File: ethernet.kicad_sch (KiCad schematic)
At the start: 38 parts, among them IC1 ACPL-217-500E, J6 5-2337992-8, U22 TPS2372-3RGWR, U23 ULS-12{slash}5-D48N-C

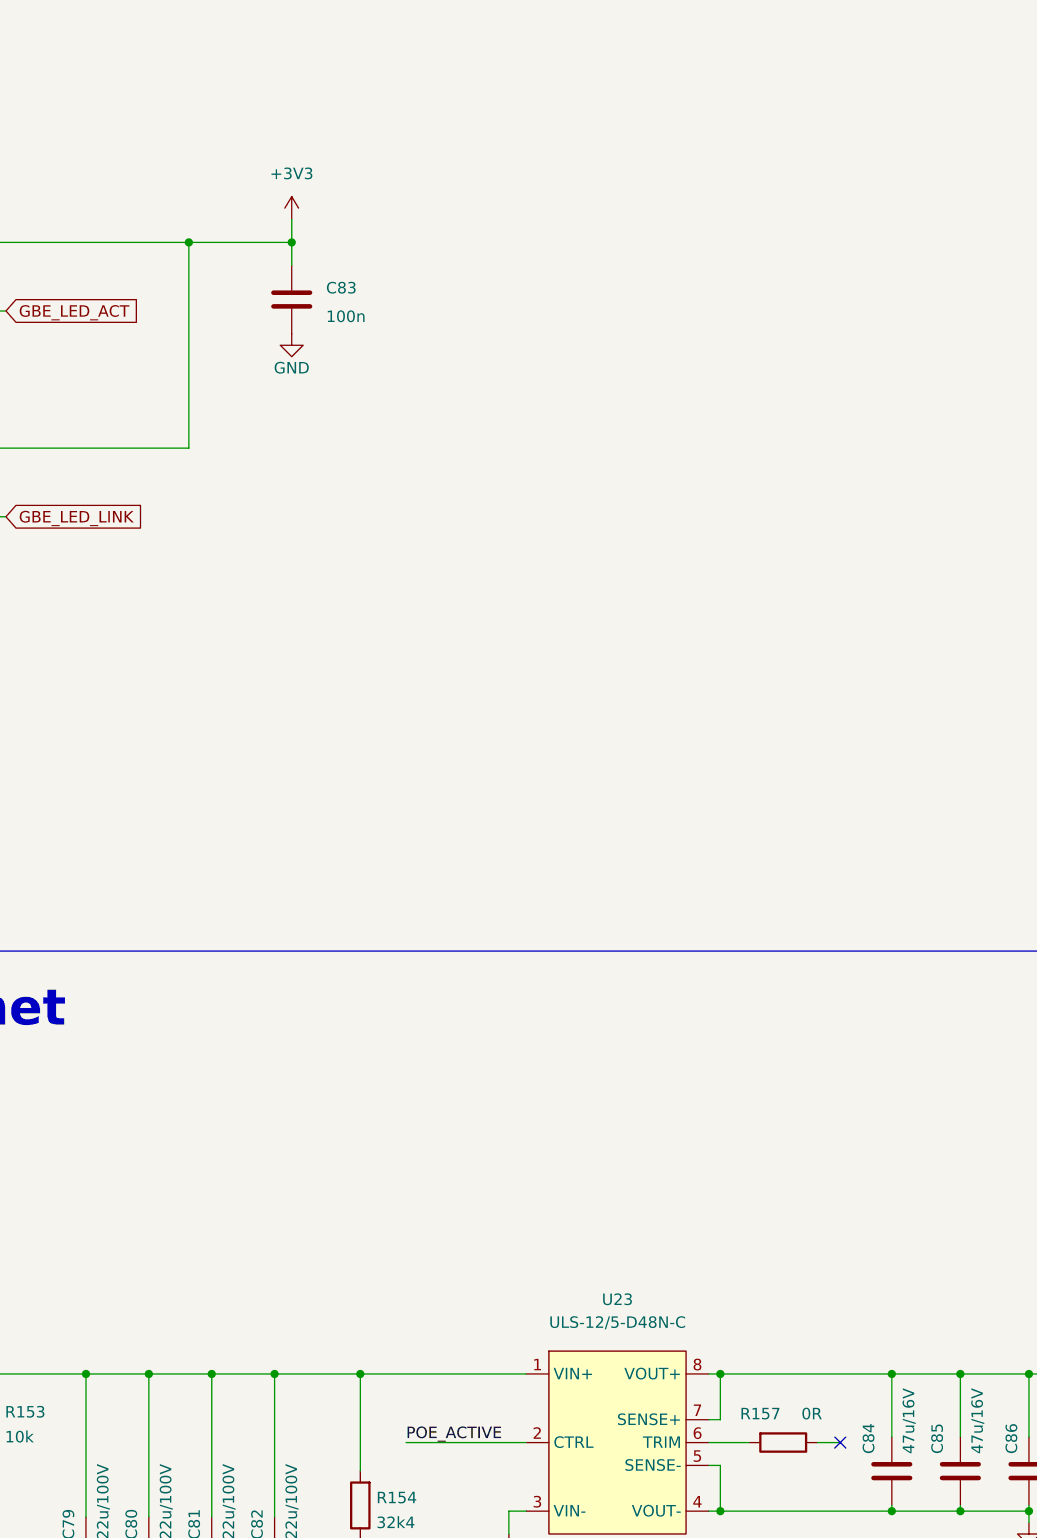
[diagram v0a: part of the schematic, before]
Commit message: Remove 100n cap from led supply
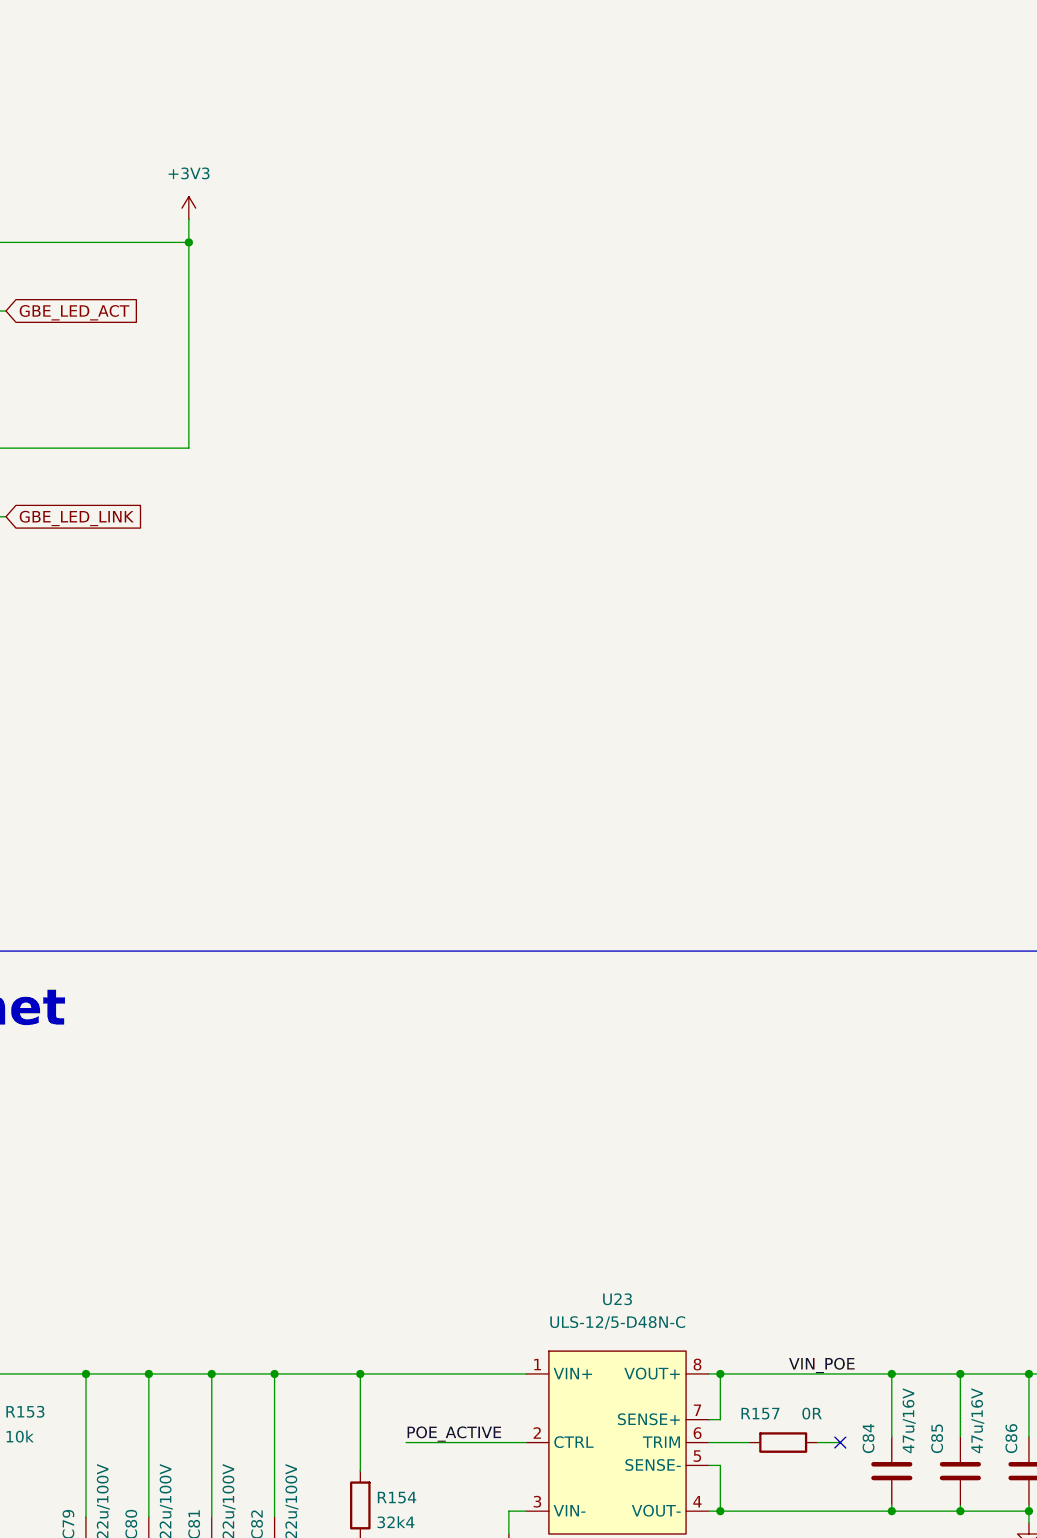
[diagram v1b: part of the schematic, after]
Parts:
- removed C83: C_100n_0402, antmicro-footprints:0402-cap, symbol antmicroCapacitors0402:C_100n_0402
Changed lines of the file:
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@@
   (junction (at 332.105 181.61) (diameter 0) (color 0 0 0 0)
   )
-  (junction (at 257.81 55.88) (diameter 0) (color 0 0 0 0)
-  )
   (junction (at 332.105 196.85) (diameter 0) (color 0 0 0 0)
   )
@@
     (stroke (width 0) (type default) (color 0 0 0 0))
   )
-  (wire (pts (xy 257.81 55.88) (xy 257.81 58.42))
-    (stroke (width 0) (type default) (color 0 0 0 0))
-  )
   (wire (pts (xy 106.68 212.09) (xy 116.84 212.09))
     (stroke (width 0) (type default) (color 0 0 0 0))
@@
     (stroke (width 0) (type default) (color 0 0 0 0))
   )
-  (wire (pts (xy 257.81 53.34) (xy 257.81 55.88))
+  (wire (pts (xy 246.38 53.34) (xy 246.38 55.88))
     (stroke (width 0) (type default) (color 0 0 0 0))
   )
@@
     (stroke (width 0) (type default) (color 0 0 0 0))
   )
-  (wire (pts (xy 246.38 55.88) (xy 257.81 55.88))
-    (stroke (width 0) (type default) (color 0 0 0 0))
-  )
   (wire (pts (xy 314.325 222.25) (xy 314.325 223.52))
     (stroke (width 0) (type default) (color 0 0 0 0))
@@
     (effects (font (size 1.27 1.27)) (justify left bottom))
   )
+  (label "VIN_POE" (at 313.055 181.61 0)
+    (effects (font (size 1.27 1.27)) (justify left bottom))
+  )
   (label "PAIR_12" (at 152.4 73.66 0)
     (effects (font (size 1.27 1.27)) (justify left bottom))
@@
     (pin "1")
   )
-  (symbol (lib_id "antmicroCapacitors0402:C_100n_0402") (at 257.81 62.23 0) (unit 1)
-    (in_bom yes) (on_board yes) (fields_autoplaced)
-    (property "Reference" "C83" (id 0) (at 261.62 60.96 0)
-      (effects (font (size 1.27 1.27)) (justify left))
-    )
-    (property "Value" "C_100n_0402" (id 1) (at 257.81 66.04 0)
-      (effects (font (size 1.27 1.27)) hide)
-    )
-    (property "Footprint" "antmicro-footprints:0402-cap" (id 2) (at 262.89 57.15 0)
-      (effects (font (size 1.524 1.524)) (justify left) hide)
-    )
-    (property "Datasheet" "" (id 3) (at 257.81 62.23 0)
-      (effects (font (size 1.27 1.27)) hide)
-    )
-    (property "Manufacturer" "Murata" (id 4) (at 262.89 52.07 0)
-      (effects (font (size 1.524 1.524)) (justify left) hide)
-    )
-    (property "MPN" "GRM155R61H104KE14D" (id 5) (at 262.89 54.61 0)
-      (effects (font (size 1.524 1.524)) (justify left) hide)
-    )
-    (property "Val" "100n" (id 6) (at 261.62 64.1349 0)
-      (effects (font (size 1.27 1.27)) (justify left))
-    )
-    (pin "1")
-    (pin "2")
-  )
   (symbol (lib_name "BLM21PG221SN1D_1") (lib_id "antmicroFerriteBeadsandChips:BLM21PG221SN1D") (at 101.6 212.09 0) (unit 1)
     (in_bom yes) (on_board yes) (fields_autoplaced)
@@
     (pin "1")
   )
-  (symbol (lib_id "power:+3V3") (at 257.81 53.34 0) (unit 1)
+  (symbol (lib_id "power:+3V3") (at 246.38 53.34 0) (unit 1)
     (in_bom yes) (on_board yes) (fields_autoplaced)
-    (property "Reference" "#PWR0142" (id 0) (at 257.81 57.15 0)
+    (property "Reference" "#PWR0142" (id 0) (at 246.38 57.15 0)
       (effects (font (size 1.27 1.27)) hide)
     )
-    (property "Value" "+3V3" (id 1) (at 257.81 48.26 0))
-    (property "Footprint" "" (id 2) (at 257.81 53.34 0)
+    (property "Value" "+3V3" (id 1) (at 246.38 48.26 0))
+    (property "Footprint" "" (id 2) (at 246.38 53.34 0)
       (effects (font (size 1.27 1.27)) hide)
     )
-    (property "Datasheet" "" (id 3) (at 257.81 53.34 0)
+    (property "Datasheet" "" (id 3) (at 246.38 53.34 0)
       (effects (font (size 1.27 1.27)) hide)
     )
@@
     (pin "2")
   )
-  (symbol (lib_id "power:GND") (at 257.81 66.04 0) (unit 1)
-    (in_bom yes) (on_board yes) (fields_autoplaced)
-    (property "Reference" "#PWR0143" (id 0) (at 257.81 72.39 0)
-      (effects (font (size 1.27 1.27)) hide)
-    )
-    (property "Value" "GND" (id 1) (at 257.81 69.85 0))
-    (property "Footprint" "" (id 2) (at 257.81 66.04 0)
-      (effects (font (size 1.27 1.27)) hide)
-    )
-    (property "Datasheet" "" (id 3) (at 257.81 66.04 0)
-      (effects (font (size 1.27 1.27)) hide)
-    )
-    (pin "1")
-  )
   (symbol (lib_id "antmicroCapacitorsmisc:C_47u_16V_1206") (at 332.105 192.405 0) (unit 1)

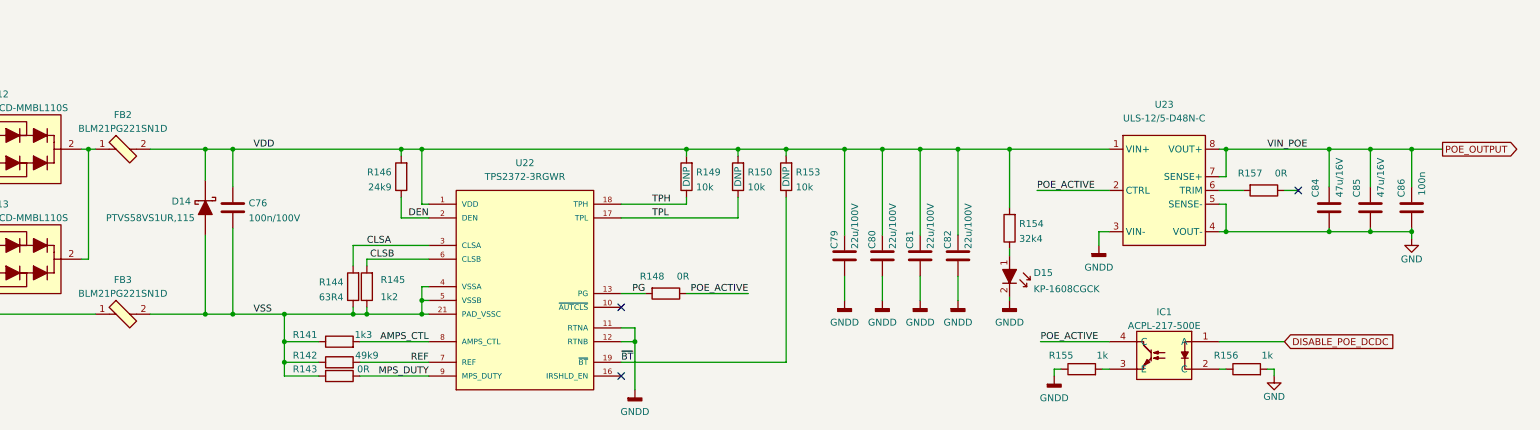
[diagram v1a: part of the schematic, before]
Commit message: Aligned everything to 50mil grid
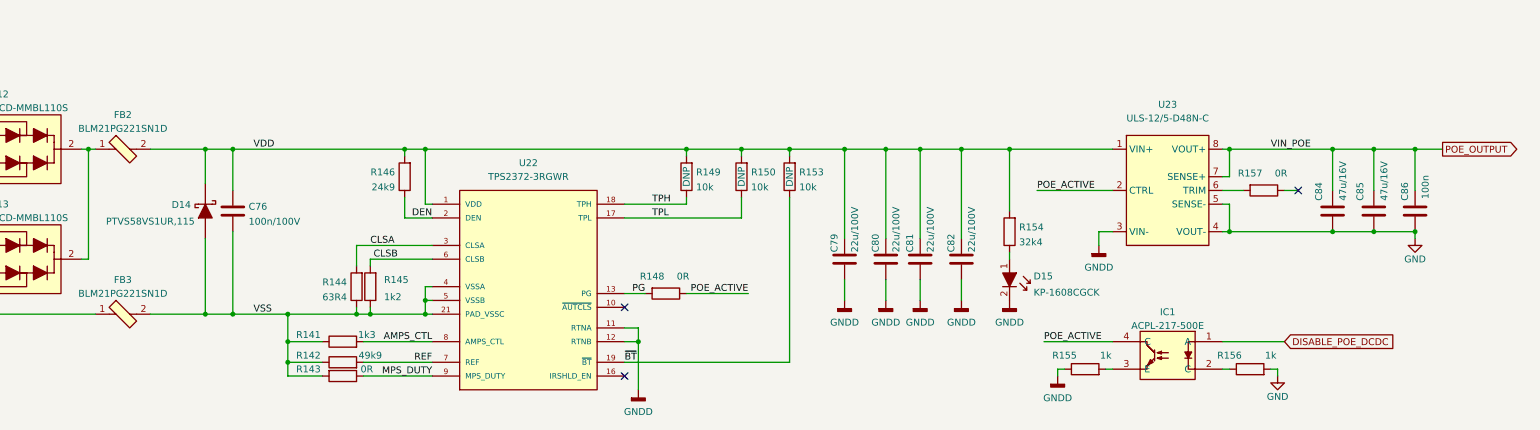
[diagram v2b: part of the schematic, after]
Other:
- moved on the sheet: C76, C79, C80, C81, C82, C84, C85, C86, D14, D15, IC1, R141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

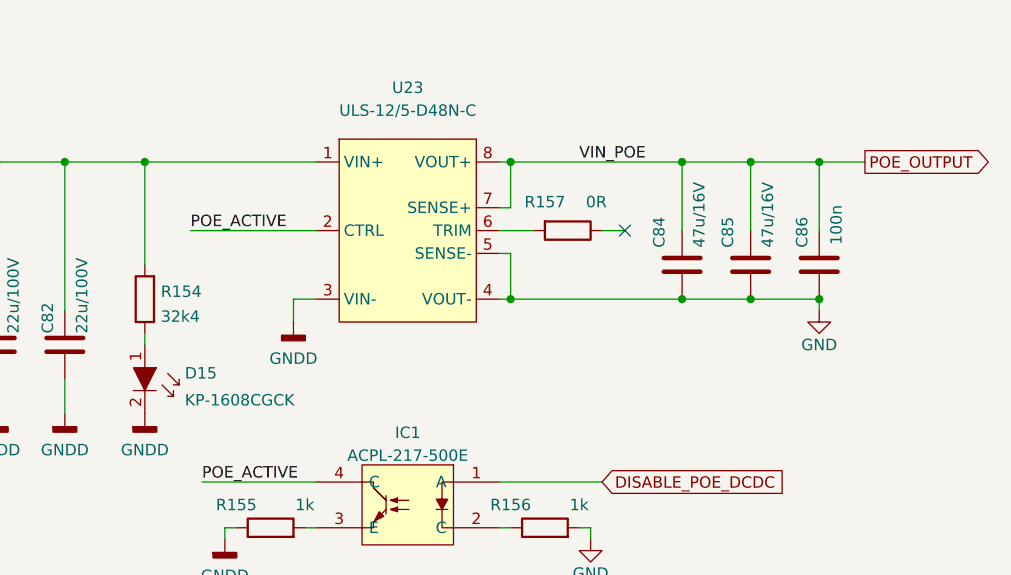
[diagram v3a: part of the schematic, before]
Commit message: Removed CSI mux LEDs and unified component types
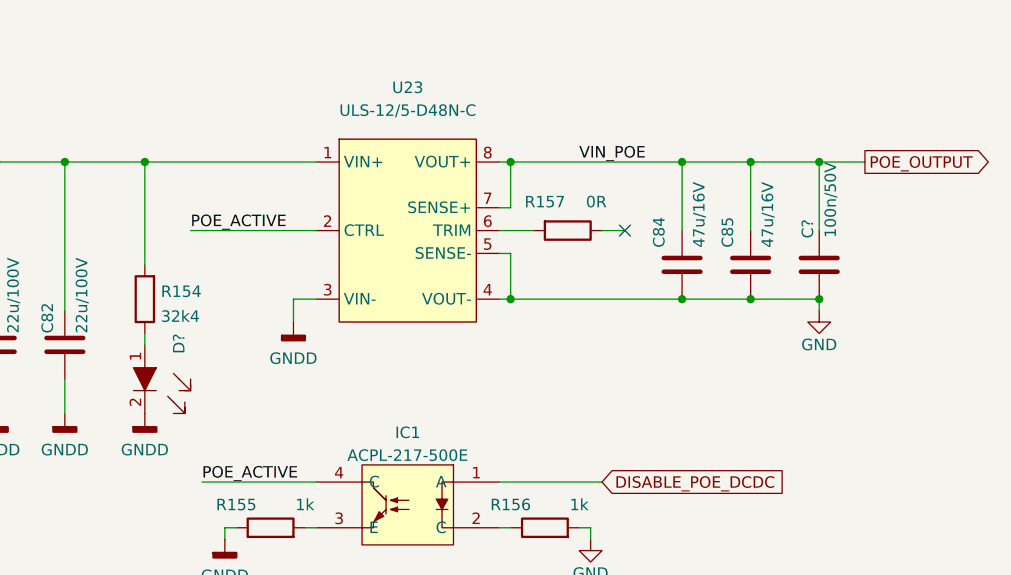
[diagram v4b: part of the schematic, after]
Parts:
- removed C86: C_100n_0402_16V, antmicro-footprints:0402-cap, symbol antmicroCapacitorsmisc:C_100n_0402_16V
- removed D15: KP-1608CGCK, antmicro-footprints:LED_0603, symbol antmicroLEDIndicationDiscrete:KP-1608CGCK
- added C?: C_100n_0402_50V, antmicro-footprints:0402-cap, symbol antmicroCapacitorsmisc:C_100n_0402_50V
- added D?: LTST-C190GKT, antmicro-footprints:LED_0603, symbol antmicroLEDIndicationDiscrete:LTST-C190GKT
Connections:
- net GND: now also C?.2
- net GNDD: now also D?.2
- net POE_OUTPUT: now also C?.1
- net at R154.1: now also D?.1
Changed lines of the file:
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@@
   (junction (at 325.12 196.85) (diameter 0) (color 0 0 0 0)
   )
+  (junction (at 340.36 196.85) (diameter 0) (color 0 0 0 0)
+  )
   (junction (at 116.84 181.61) (diameter 0) (color 0 0 0 0)
   )
@@
   (junction (at 157.48 181.61) (diameter 0) (color 0 0 0 0)
   )
-  (junction (at 340.36 196.85) (diameter 0) (color 0 0 0 0)
-  )
   (junction (at 332.74 181.61) (diameter 0) (color 0 0 0 0)
   )
@@
     (pin "2")
   )
-  (symbol (lib_id "antmicroLEDIndicationDiscrete:KP-1608CGCK") (at 265.43 207.01 270) (unit 1)
-    (in_bom yes) (on_board yes) (fields_autoplaced)
-    (property "Reference" "D15" (id 0) (at 269.875 205.0813 90)
-      (effects (font (size 1.27 1.27)) (justify left))
-    )
-    (property "Value" "KP-1608CGCK" (id 1) (at 269.875 208.0747 90)
-      (effects (font (size 1.27 1.27)) (justify left))
-    )
-    (property "Footprint" "antmicro-footprints:LED_0603" (id 2) (at 270.51 212.09 0)
-      (effects (font (size 1.524 1.524)) (justify left) hide)
-    )
-    (property "Datasheet" "http://www.farnell.com/datasheets/2045956.pdf" (id 3) (at 273.05 212.09 0)
-      (effects (font (size 1.524 1.524)) (justify left) hide)
-    )
-    (property "MPN" "KP-1608CGCK" (id 4) (at 278.13 212.09 0)
-      (effects (font (size 1.524 1.524)) (justify left) hide)
-    )
-    (property "Manufacturer" "KINGBRIGHT" (id 5) (at 281.178 212.344 0)
-      (effects (font (size 1.524 1.524)) (justify left) hide)
-    )
-    (pin "1")
-    (pin "2")
-  )
   (symbol (lib_id "antmicroCapacitorsmisc:C_22u_2220_100V") (at 234.95 201.93 0) (unit 1)
     (in_bom yes) (on_board yes)
@@
     (pin "1")
   )
-  (symbol (lib_id "antmicroCapacitorsmisc:C_100n_0402_16V") (at 340.36 193.04 0) (unit 1)
-    (in_bom yes) (on_board yes)
-    (property "Reference" "C86" (id 0) (at 338.455 191.135 90)
-      (effects (font (size 1.27 1.27)) (justify left))
-    )
-    (property "Value" "C_100n_0402_16V" (id 1) (at 340.36 196.85 0)
-      (effects (font (size 1.27 1.27)) hide)
-    )
-    (property "Footprint" "antmicro-footprints:0402-cap" (id 2) (at 345.44 187.96 0)
-      (effects (font (size 1.524 1.524)) (justify left) hide)
-    )
-    (property "Datasheet" "" (id 3) (at 340.36 193.04 0)
-      (effects (font (size 1.27 1.27)) hide)
-    )
-    (property "Manufacturer" "MULTICOMP" (id 4) (at 345.44 182.88 0)
-      (effects (font (size 1.524 1.524)) (justify left) hide)
-    )
-    (property "MPN" "MC0402B104K160CT" (id 5) (at 345.44 185.42 0)
-      (effects (font (size 1.524 1.524)) (justify left) hide)
-    )
-    (property "Val" "100n" (id 6) (at 342.265 188.595 90))
-    (pin "1")
-    (pin "2")
-  )
   (symbol (lib_id "antmicroResistors0402:R_10k_0402") (at 205.74 186.69 90) (unit 1)
     (in_bom yes) (on_board yes)
@@
     (pin "2")
   )
+  (symbol (lib_id "antmicroCapacitorsmisc:C_100n_0402_50V") (at 340.36 193.04 0) (mirror y) (unit 1)
+    (in_bom yes) (on_board yes)
+    (property "Reference" "C?" (id 0) (at 339.09 187.96 90)
+      (effects (font (size 1.27 1.27)) (justify right))
+    )
+    (property "Value" "C_100n_0402_50V" (id 1) (at 340.36 193.04 0)
+      (effects (font (size 1.27 1.27)) hide)
+    )
+    (property "Footprint" "antmicro-footprints:0402-cap" (id 2) (at 340.36 193.04 0)
+      (effects (font (size 1.27 1.27)) hide)
+    )
+    (property "Datasheet" "" (id 3) (at 340.36 193.04 0)
+      (effects (font (size 1.27 1.27)) hide)
+    )
+    (property "MPN" "GRM155R71H104KE14D" (id 4) (at 340.36 193.04 0)
+      (effects (font (size 1.27 1.27)) hide)
+    )
+    (property "Manufacturer" "MURATA" (id 5) (at 340.36 193.04 0)
+      (effects (font (size 1.27 1.27)) hide)
+    )
+    (property "Val" "100n/50V" (id 6) (at 341.63 181.61 90)
+      (effects (font (size 1.27 1.27)) (justify right))
+    )
+    (pin "1")
+    (pin "2")
+  )
   (symbol (lib_id "antmicroResistors0603:R_1k_0603") (at 279.4 222.25 0) (unit 1)
     (in_bom yes) (on_board yes)
@@
     )
     (pin "1")
+    (pin "2")
+  )
+  (symbol (lib_id "antmicroLEDIndicationDiscrete:LTST-C190GKT") (at 265.43 207.01 270) (unit 1)
+    (in_bom yes) (on_board yes)
+    (property "Reference" "D?" (id 0) (at 269.24 200.66 0)
+      (effects (font (size 1.27 1.27)) (justify left))
+    )
+    (property "Value" "LTST-C190GKT" (id 1) (at 261.62 207.01 0)
+      (effects (font (size 1.27 1.27)) hide)
+    )
+    (property "Footprint" "antmicro-footprints:LED_0603" (id 2) (at 270.51 212.09 0)
+      (effects (font (size 1.524 1.524)) (justify left) hide)
+    )
+    (property "Datasheet" "https://media.digikey.com/pdf/Data%20Sheets/Lite-On%20PDFs/LTST-C190GKT.pdf" (id 3) (at 273.05 212.09 0)
+      (effects (font (size 1.524 1.524)) (justify left) hide)
+    )
+    (property "MPN" "LTST-C190GKT" (id 4) (at 278.13 212.09 0)
+      (effects (font (size 1.524 1.524)) (justify left) hide)
+    )
+    (property "Manufacturer" "Lite-On Inc." (id 5) (at 293.37 212.09 0)
+      (effects (font (size 1.524 1.524)) (justify left) hide)
+    )
+    (pin "1")
